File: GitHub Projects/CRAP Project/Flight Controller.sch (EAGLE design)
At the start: 12 parts, among them J1 2POS_SCREWTERM, J2 4POS_SCREWTERM, J3 4POS_SCREWTERM, J4 4POS_SCREWTERM, J5 4POS_SCREWTERM

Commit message: Routed more, added GPS
1. Added Antenova library
2. Added our GPS to the Antenova library
3. Placed GPS, which caused our power system to move, also increased
board height by 5mm due to expected space constraints
4. Moved our power system close to the Xbee
5. Placed a MOSFET for the separation circuit
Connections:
- net +3V3: now also C3.2
- net N$2: now also C2.1
- net N$3: now also C1.1

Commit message: Routing, schematic changes
1. Changed some schematic errors on the firing chains
2. Routed more GPS, changed inductor on power supply, routed Xbee
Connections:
- removed net FC2+: J3.P3
- removed net FC4+: J4.P3
- net +12V: now also J3.P3, J4.P3

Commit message: More routing changes
1. Changed the power circuit 180 degrees to better fit the inductor
2. Routed a lot of the ordance circuits and placed all MOSFETS
3. Routed lots of power
4. Oh god it's so crowded
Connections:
- net FC3- renamed FC1-2
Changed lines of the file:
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@@
 <setting verticaltext="up"/>
 </settings>
-<grid distance="0.1" unitdist="inch" unit="inch" style="lines" multiple="1" display="yes" altdistance="0.01" altunitdist="inch" altunit="inch"/>
+<grid distance="0.1" unitdist="inch" unit="inch" style="lines" multiple="1" display="no" altdistance="0.01" altunitdist="inch" altunit="inch"/>
 <layers>
 <layer number="1" name="Top" color="4" fill="1" visible="no" active="no"/>
@@
 </segment>
 </net>
-<net name="FC3-" class="0">
-<segment>
-<wire x1="218.44" y1="55.88" x2="218.44" y2="29.21" width="0.1524" layer="91"/>
-<pinref part="J4" gate="G$1" pin="P2"/>
-<wire x1="228.6" y1="29.21" x2="218.44" y2="29.21" width="0.1524" layer="91"/>
-<label x="223.52" y="29.21" size="1.778" layer="95"/>
-</segment>
-</net>
 <net name="FC1-" class="0">
 <segment>
@@
 <junction x="210.82" y="55.88"/>
 <label x="156.21" y="31.75" size="1.778" layer="95" xref="yes"/>
-</segment>
-</net>
+<pinref part="J4" gate="G$1" pin="P2"/>
+<wire x1="218.44" y1="55.88" x2="218.44" y2="29.21" width="0.1524" layer="91"/>
+<wire x1="218.44" y1="29.21" x2="228.6" y2="29.21" width="0.1524" layer="91"/>
+<label x="223.52" y="29.21" size="1.778" layer="95"/>
+</segment>
+</net>

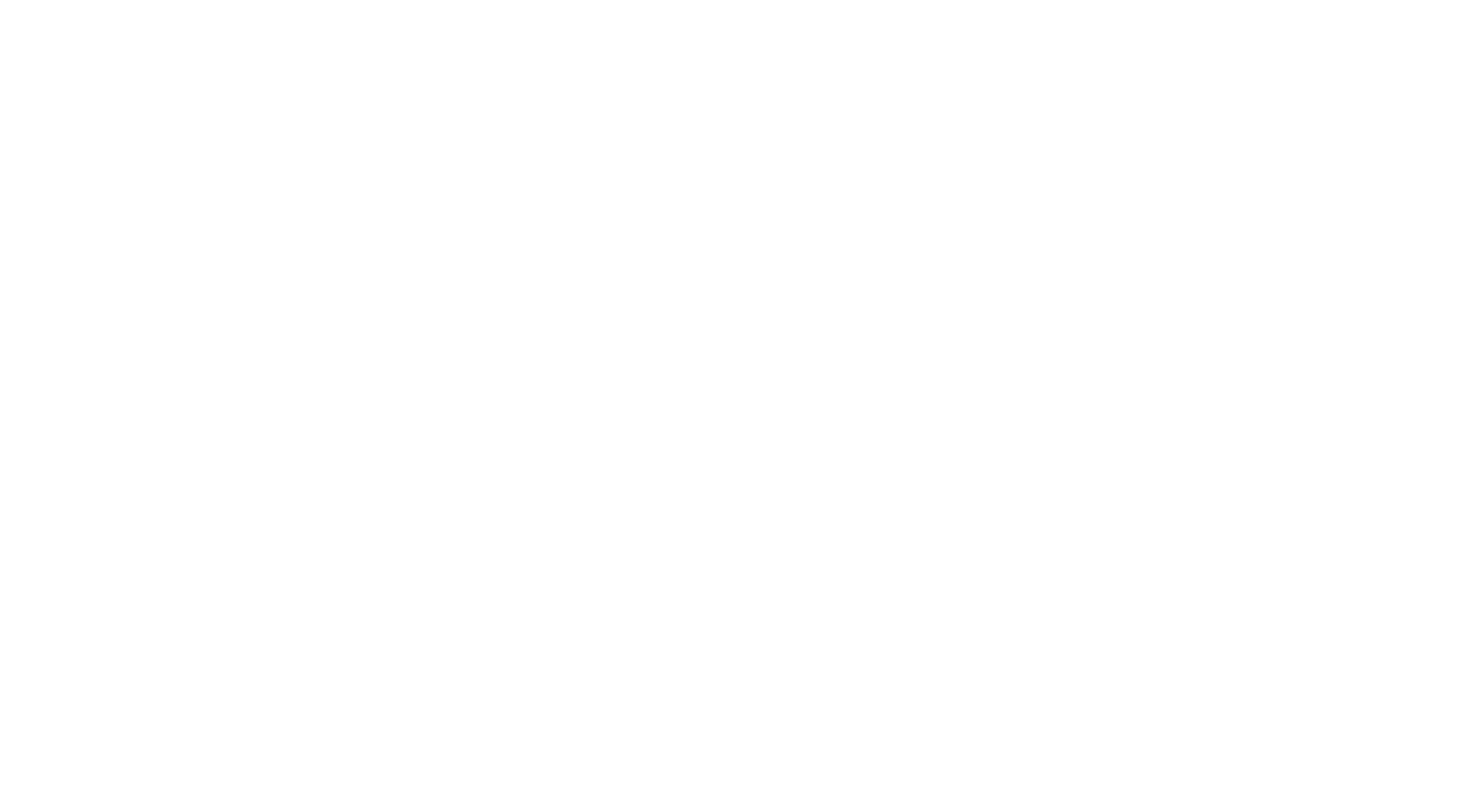
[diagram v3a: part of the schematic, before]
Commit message: More routing
1. Routed parts of the ordance
2. Routed parts of the RTD
3. Routed Parts of the breakwire
4. Swapped RTD and breakwire headers to allow for actual routing because
it was too cramped to fit the RTD's sensor chip in the area that the
header was in
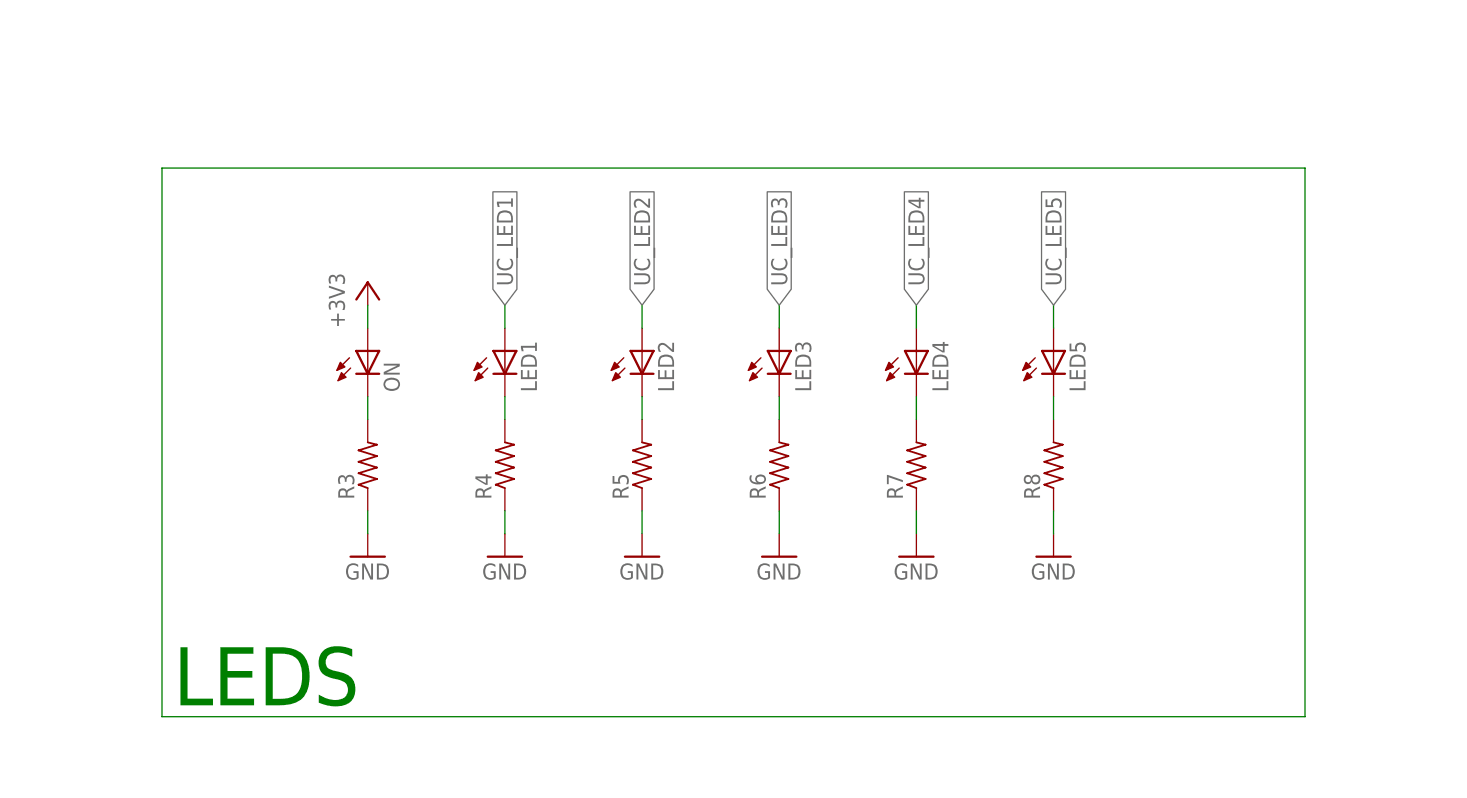
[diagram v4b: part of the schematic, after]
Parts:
- added LED1, LED2, LED3, LED4, LED5, ON: (no value), led:LEDCHIPLED_0603
- added R3, R4, R5, R6, R7, R8: (no value), rcl:R-US_R0603
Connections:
- new net !CONT_EN: R4.1
- new net 3V3_OUT: R3.2, R5.2
- new net FIRE1: R3.2
- new net N$24: LED1.C, R4.2
- new net N$25: LED2.C, R5.2
- new net N$26: LED3.C, R6.2
- new net N$27: LED4.C, R7.2
- new net N$28: LED5.C, R8.2
- new net N$30: ON.C, R3.2
- new net UC_LED1: LED1.A
- new net UC_LED2: LED2.A
- new net UC_LED3: LED3.A
- new net UC_LED4: LED4.A
- new net UC_LED5: LED5.A
- net +3V3: now also ON.A, R3.2, R4.2
- net CONT_STAT/PYRO–: now also R5.1
- net GND: now also R3.1, R4.1, R5.1, R6.1, R7.1, R8.1
- net N$1: now also R3.2, R4.2
- net N$10: now also R3.1, R4.2
- net N$11: now also R6.1
- net N$4: now also R3.1
- net N$5: now also R4.1
- net N$6: now also R3.2
- net N$9: now also R5.1
- net PWR/PYRO+: now also R5.2
- net SDA: now also R3.1
- net VIN: now also R6.2
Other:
- note added: "LEDS"
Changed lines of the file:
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@@
 <part name="U1" library="linear-technology" deviceset="LTC3225" device=""/>
 <part name="C1" library="rcl" deviceset="C-EU" device="C0805" value="2.2u"/>
-<part name="C2" library="rcl" deviceset="C-EU" device="C0805" value="1u"/>
+<part name="C2" library="rcl" deviceset="C-EU" device="C0402" value="1u"/>
 <part name="C3" library="rcl" deviceset="C-EU" device="C0603" value="1u"/>
 <part name="R1" library="resistor" deviceset="R-US_" device="R0603" value="10k"/>
@@
 <part name="+3V10" library="supply1" deviceset="+3V3" device=""/>
 <part name="+3V11" library="supply1" deviceset="+3V3" device=""/>
+<part name="ON" library="led" deviceset="LED" device="CHIPLED_0603"/>
+<part name="LED1" library="led" deviceset="LED" device="CHIPLED_0603"/>
+<part name="LED2" library="led" deviceset="LED" device="CHIPLED_0603"/>
+<part name="LED3" library="led" deviceset="LED" device="CHIPLED_0603"/>
+<part name="LED4" library="led" deviceset="LED" device="CHIPLED_0603"/>
+<part name="LED5" library="led" deviceset="LED" device="CHIPLED_0603"/>
+<part name="R3" library="rcl" deviceset="R-US_" device="R0603"/>
+<part name="R4" library="rcl" deviceset="R-US_" device="R0603"/>
+<part name="R5" library="rcl" deviceset="R-US_" device="R0603"/>
+<part name="R6" library="rcl" deviceset="R-US_" device="R0603"/>
+<part name="R7" library="rcl" deviceset="R-US_" device="R0603"/>
+<part name="R8" library="rcl" deviceset="R-US_" device="R0603"/>
+<part name="+3V17" library="supply1" deviceset="+3V3" device=""/>
+<part name="GND19" library="supply1" deviceset="GND" device=""/>
+<part name="GND20" library="supply1" deviceset="GND" device=""/>
+<part name="GND21" library="supply1" deviceset="GND" device=""/>
+<part name="GND22" library="supply1" deviceset="GND" device=""/>
+<part name="GND23" library="supply1" deviceset="GND" device=""/>
+<part name="GND24" library="supply1" deviceset="GND" device=""/>
 </parts>
 <sheets>
@@
 <text x="60.96" y="-6.35" size="1.778" layer="97">USART7 Module</text>
 <text x="60.96" y="31.75" size="1.778" layer="97">USART5 Module</text>
+<text x="-49.53" y="-186.69" size="6.4516" layer="91">LEDS</text>
 </plain>
 <moduleinsts>
@@
 <instance part="+3V10" gate="G$1" x="180.34" y="134.62"/>
 <instance part="+3V11" gate="G$1" x="185.42" y="198.12"/>
+<instance part="ON" gate="G$1" x="-27.94" y="-147.32"/>
+<instance part="LED1" gate="G$1" x="-12.7" y="-147.32"/>
+<instance part="LED2" gate="G$1" x="2.54" y="-147.32"/>
+<instance part="LED3" gate="G$1" x="17.78" y="-147.32"/>
+<instance part="LED4" gate="G$1" x="33.02" y="-147.32"/>
+<instance part="LED5" gate="G$1" x="48.26" y="-147.32"/>
+<instance part="R3" gate="G$1" x="-27.94" y="-160.02" rot="R90"/>
+<instance part="R4" gate="G$1" x="-12.7" y="-160.02" rot="R90"/>
+<instance part="R5" gate="G$1" x="2.54" y="-160.02" rot="R90"/>
+<instance part="R6" gate="G$1" x="17.78" y="-160.02" rot="R90"/>
+<instance part="R7" gate="G$1" x="33.02" y="-160.02" rot="R90"/>
+<instance part="R8" gate="G$1" x="48.26" y="-160.02" rot="R90"/>
+<instance part="+3V17" gate="G$1" x="-27.94" y="-139.7"/>
+<instance part="GND19" gate="1" x="48.26" y="-170.18"/>
+<instance part="GND20" gate="1" x="33.02" y="-170.18"/>
+<instance part="GND21" gate="1" x="17.78" y="-170.18"/>
+<instance part="GND22" gate="1" x="2.54" y="-170.18"/>
+<instance part="GND23" gate="1" x="-12.7" y="-170.18"/>
+<instance part="GND24" gate="1" x="-27.94" y="-170.18"/>
 </instances>
 <busses>
@@
 <wire x1="-241.3" y1="-45.72" x2="-241.3" y2="-43.18" width="0.1524" layer="91"/>
 </segment>
+<segment>
+<pinref part="R3" gate="G$1" pin="1"/>
+<pinref part="GND24" gate="1" pin="GND"/>
+<wire x1="-27.94" y1="-165.1" x2="-27.94" y2="-167.64" width="0.1524" layer="91"/>
+</segment>
+<segment>
+<pinref part="R4" gate="G$1" pin="1"/>
+<pinref part="GND23" gate="1" pin="GND"/>
+<wire x1="-12.7" y1="-165.1" x2="-12.7" y2="-167.64" width="0.1524" layer="91"/>
+</segment>
+<segment>
+<pinref part="GND22" gate="1" pin="GND"/>
+<pinref part="R5" gate="G$1" pin="1"/>
+<wire x1="2.54" y1="-167.64" x2="2.54" y2="-165.1" width="0.1524" layer="91"/>
+</segment>
+<segment>
+<pinref part="R6" gate="G$1" pin="1"/>
+<pinref part="GND21" gate="1" pin="GND"/>
+<wire x1="17.78" y1="-165.1" x2="17.78" y2="-167.64" width="0.1524" layer="91"/>
+</segment>
+<segment>
+<pinref part="GND20" gate="1" pin="GND"/>
+<pinref part="R7" gate="G$1" pin="1"/>
+<wire x1="33.02" y1="-167.64" x2="33.02" y2="-165.1" width="0.1524" layer="91"/>
+</segment>
+<segment>
+<pinref part="R8" gate="G$1" pin="1"/>
+<pinref part="GND19" gate="1" pin="GND"/>
+<wire x1="48.26" y1="-165.1" x2="48.26" y2="-167.64" width="0.1524" layer="91"/>
+</segment>
 </net>
 <net name="+3V3" class="0">
@@
 <wire x1="-147.32" y1="-12.7" x2="-147.32" y2="-10.16" width="0.1524" layer="91"/>
 </segment>
+<segment>
+<pinref part="ON" gate="G$1" pin="A"/>
+<wire x1="-27.94" y1="-144.78" x2="-27.94" y2="-142.24" width="0.1524" layer="91"/>
+<pinref part="+3V17" gate="G$1" pin="+3V3"/>
+</segment>
 </net>
 <net name="VCC_IN" class="0">
@@
 </segment>
 </net>
+<net name="N$16" class="0">
+<segment>
+<wire x1="-50.8" y1="-187.96" x2="76.2" y2="-187.96" width="0.1524" layer="91"/>
+<wire x1="76.2" y1="-187.96" x2="76.2" y2="-127" width="0.1524" layer="91"/>
+<wire x1="76.2" y1="-127" x2="-50.8" y2="-127" width="0.1524" layer="91"/>
+<wire x1="-50.8" y1="-127" x2="-50.8" y2="-187.96" width="0.1524" layer="91"/>
+</segment>
+</net>
+<net name="N$24" class="0">
+<segment>
+<pinref part="LED1" gate="G$1" pin="C"/>
+<wire x1="-12.7" y1="-152.4" x2="-12.7" y2="-154.94" width="0.1524" layer="91"/>
+<pinref part="R4" gate="G$1" pin="2"/>
+</segment>
+</net>
+<net name="N$25" class="0">
+<segment>
+<pinref part="LED2" gate="G$1" pin="C"/>
+<wire x1="2.54" y1="-152.4" x2="2.54" y2="-154.94" width="0.1524" layer="91"/>
+<pinref part="R5" gate="G$1" pin="2"/>
+</segment>
+</net>
+<net name="N$26" class="0">
+<segment>
+<pinref part="LED3" gate="G$1" pin="C"/>
+<wire x1="17.78" y1="-152.4" x2="17.78" y2="-154.94" width="0.1524" layer="91"/>
+<pinref part="R6" gate="G$1" pin="2"/>
+</segment>
+</net>
+<net name="N$27" class="0">
+<segment>
+<pinref part="LED4" gate="G$1" pin="C"/>
+<wire x1="33.02" y1="-152.4" x2="33.02" y2="-154.94" width="0.1524" layer="91"/>
+<pinref part="R7" gate="G$1" pin="2"/>
+</segment>
+</net>
+<net name="N$28" class="0">
+<segment>
+<pinref part="LED5" gate="G$1" pin="C"/>
+<wire x1="48.26" y1="-152.4" x2="48.26" y2="-154.94" width="0.1524" layer="91"/>
+<pinref part="R8" gate="G$1" pin="2"/>
+</segment>
+</net>
+<net name="N$30" class="0">
+<segment>
+<pinref part="ON" gate="G$1" pin="C"/>
+<wire x1="-27.94" y1="-152.4" x2="-27.94" y2="-154.94" width="0.1524" layer="91"/>
+<pinref part="R3" gate="G$1" pin="2"/>
+</segment>
+</net>
+<net name="UC_LED1" class="0">
+<segment>
+<pinref part="LED1" gate="G$1" pin="A"/>
+<wire x1="-12.7" y1="-144.78" x2="-12.7" y2="-142.24" width="0.1524" layer="91"/>
+<label x="-12.7" y="-142.24" size="1.778" layer="95" rot="R90" xref="yes"/>
+</segment>
+</net>
+<net name="UC_LED2" class="0">
+<segment>
+<pinref part="LED2" gate="G$1" pin="A"/>
+<wire x1="2.54" y1="-144.78" x2="2.54" y2="-142.24" width="0.1524" layer="91"/>
+<label x="2.54" y="-142.24" size="1.778" layer="95" rot="R90" xref="yes"/>
+</segment>
+</net>
+<net name="UC_LED3" class="0">
+<segment>
+<pinref part="LED3" gate="G$1" pin="A"/>
+<wire x1="17.78" y1="-144.78" x2="17.78" y2="-142.24" width="0.1524" layer="91"/>
+<label x="17.78" y="-142.24" size="1.778" layer="95" rot="R90" xref="yes"/>
+</segment>
+</net>
+<net name="UC_LED4" class="0">
+<segment>
+<pinref part="LED4" gate="G$1" pin="A"/>
+<wire x1="33.02" y1="-144.78" x2="33.02" y2="-142.24" width="0.1524" layer="91"/>
+<label x="33.02" y="-142.24" size="1.778" layer="95" rot="R90" xref="yes"/>
+</segment>
+</net>
+<net name="UC_LED5" class="0">
+<segment>
+<pinref part="LED5" gate="G$1" pin="A"/>
+<wire x1="48.26" y1="-144.78" x2="48.26" y2="-142.24" width="0.1524" layer="91"/>
+<label x="48.26" y="-142.24" size="1.778" layer="95" rot="R90" xref="yes"/>
+</segment>
+</net>
